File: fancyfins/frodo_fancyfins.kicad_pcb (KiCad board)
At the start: 2 copper layers, 140 x 115 mm, 102 parts, among them J3 TC2050, U1 AZ1117-5.0, U10 L78L05_SOT89, U11 W25Q128JVP, U12 L78L05_SOT89, U13 L78L05_SOT89, U14 L78L05_SOT89, U15 L78L05_SOT89, U16 L78L05_SOT89, U2 AZ1117-3.3, U3 STM32F103RCTx, U4 MCP2562-E-SN, U5 TPD4E1U06, U6 L78L05_SOT89, U7 L78L05_SOT89, U8 L78L05_SOT89, U9 L78L05_SOT89, Y1 8MHz 12pF

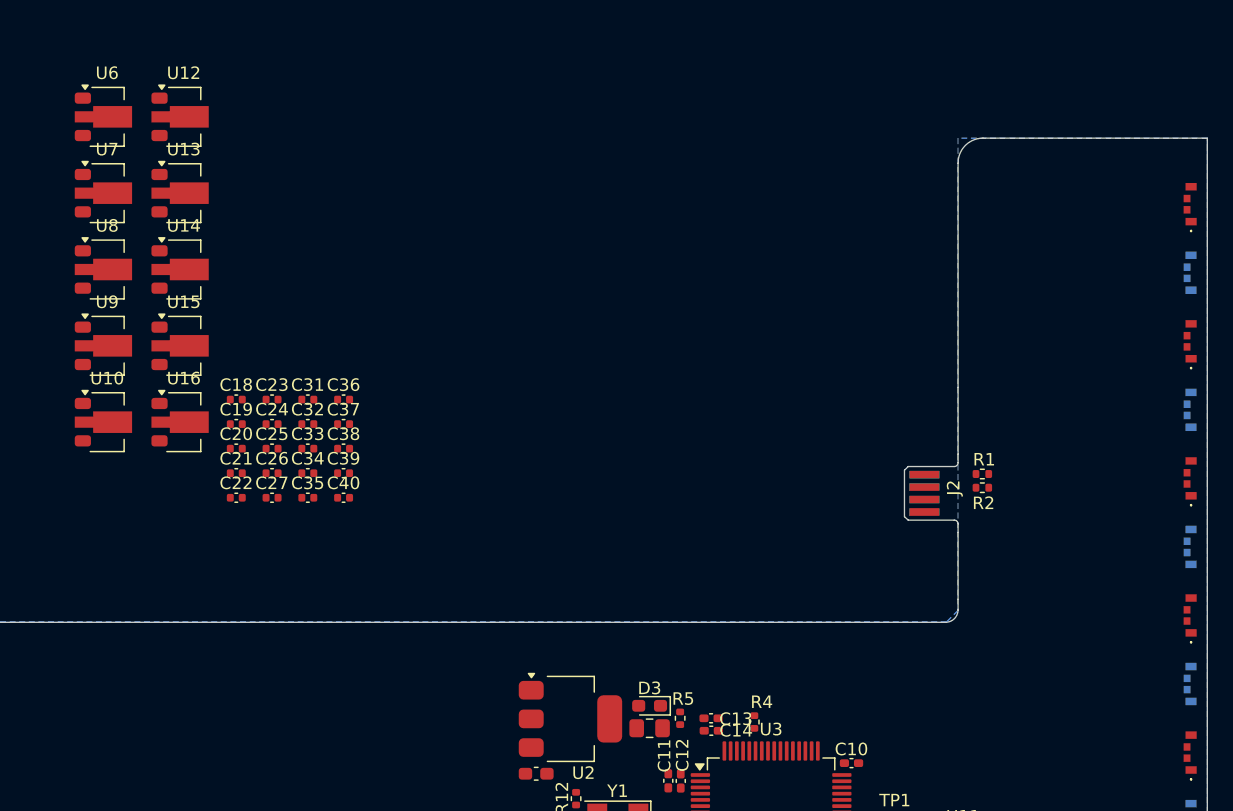
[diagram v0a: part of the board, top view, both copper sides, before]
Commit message: changed scematic + examplary layout
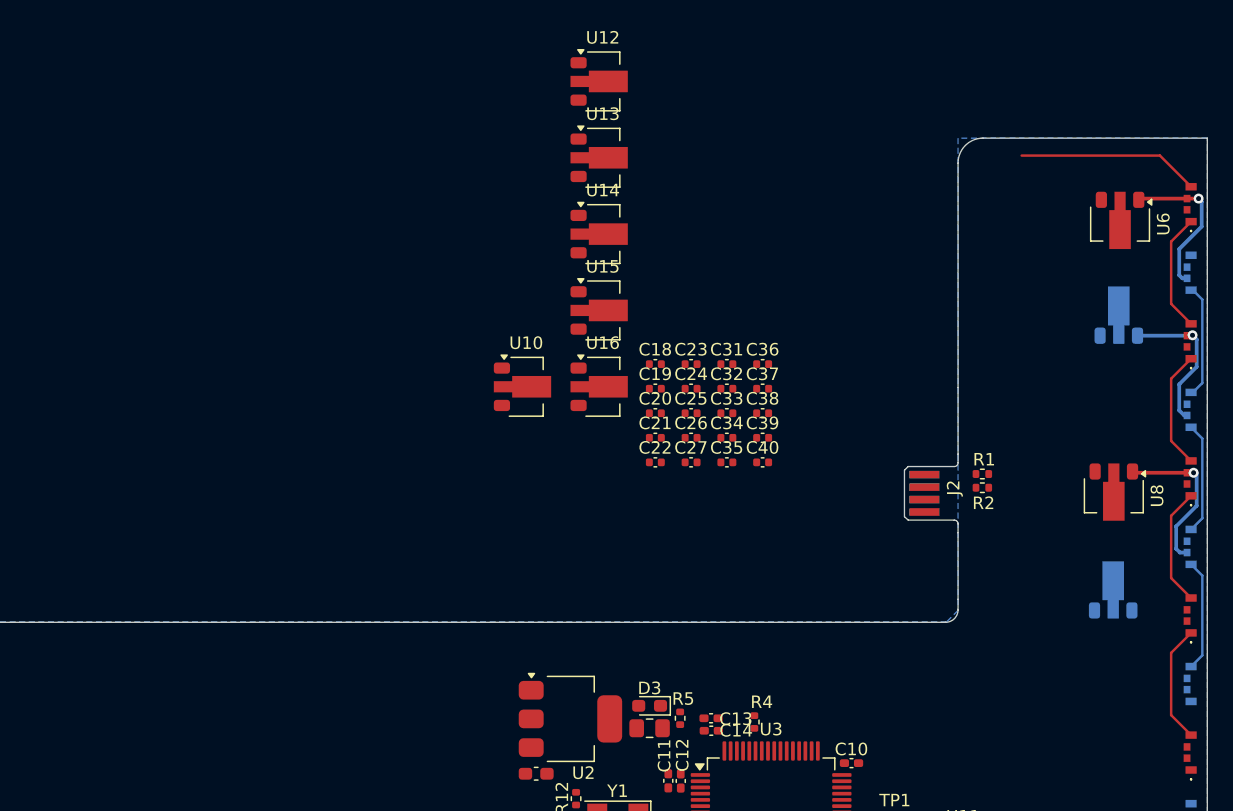
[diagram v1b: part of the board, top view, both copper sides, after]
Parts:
- U7, U9: moved to B.Cu
- moved U9 83.0 mm to (218.4, 71.0), turned to 90 degrees
- moved U8 82.8 mm to (218.5, 63.7), turned to -90 degrees
- moved U6 81.7 mm to (219.0, 41.9), turned to -90 degrees
- moved U7 81.7 mm to (218.9, 48.9), turned to 90 degrees
- moved C18 33.7 mm to (181.7, 53.1)
- moved C19 33.7 mm to (181.7, 55.1)
- moved C20 33.7 mm to (181.7, 57.1)
- moved C21 33.7 mm to (181.7, 59.0)
- moved C22 33.7 mm to (181.7, 61.0)
- moved C23 33.7 mm to (184.6, 53.1)
- moved C24 33.7 mm to (184.6, 55.1)
- moved C25 33.7 mm to (184.6, 57.1)
- moved C26 33.7 mm to (184.6, 59.0)
- moved C27 33.7 mm to (184.6, 61.0)
- moved C31 33.7 mm to (187.4, 53.1)
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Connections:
- D11 pad 4: Net-(D10-DO) -> Net-(D11-DIN)
- D12 pad 1: Net-(D12-DO) -> Net-(D10-DIN)
- D12 pad 4: Net-(D11-DO) -> Net-(D12-DIN)
- D13 pad 1: Net-(D13-DO) -> LED_Signal_cont
- D13 pad 4: Net-(D12-DO) -> Net-(D11-DO)
- D14 pad 1: LED_Signal_cont -> Net-(D12-DIN)
- D14 pad 4: Net-(D13-DO) -> LED_Signal_cont2
- D16 pad 1: Net-(D16-DO) -> LED_Signal_cont2
- D16 pad 4: Net-(D15-DO) -> Net-(D16-DIN)
- D17 pad 4: Net-(D16-DO) -> Net-(D15-DO)
- D18 pad 1: Net-(D18-DO) -> Net-(D16-DIN)
- D18 pad 4: Net-(D17-DO) -> Net-(D18-DIN)
- D19 pad 4: Net-(D18-DO) -> Net-(D17-DO)
- D20 pad 1: Net-(D20-DO) -> Net-(D18-DIN)
- D20 pad 4: Net-(D19-DO) -> Net-(D20-DIN)
- D21 pad 4: Net-(D20-DO) -> Net-(D19-DO)
- D22 pad 1: Net-(D22-DO) -> Net-(D20-DIN)
- D22 pad 4: Net-(D21-DO) -> Net-(D22-DIN)
- D23 pad 4: Net-(D22-DO) -> Net-(D21-DO)
- D24 pad 1: unconnected-(D24-DO-Pad1) -> Net-(D22-DIN)
- D6 pad 1: Net-(D6-DO) -> unconnected-(D6-DO-Pad1)
- D6 pad 4: Net-(D5-DO) -> Net-(D6-DIN)
- D7 pad 4: Net-(D6-DO) -> Net-(D5-DO)
- D8 pad 1: Net-(D8-DO) -> Net-(D6-DIN)
- D8 pad 4: Net-(D7-DO) -> Net-(D10-DO)
- D9 pad 1: Net-(D10-DIN) -> Net-(D11-DIN)
- D9 pad 4: Net-(D8-DO) -> Net-(D7-DO)
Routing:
- net LED_Signal: track 0.00 -> 14.6 mm
- net Net-(D10-VDD): track 0.00 -> 13.0 mm, vias 0 -> 1
- net Net-(D5-VDD): track 0.00 -> 12.6 mm, vias 0 -> 1
- net Net-(D7-VDD): track 0.00 -> 12.4 mm, vias 0 -> 1
- net Net-(D11-DO): track 0.00 -> 9.53 mm
- net Net-(D11-DIN): track 0.00 -> 9.53 mm
- net Net-(D7-DO): track 0.00 -> 9.53 mm
- net Net-(D5-DO): track 0.00 -> 9.53 mm
- net Net-(D6-DIN): track 0.00 -> 9.12 mm
- net Net-(D10-DIN): track 0.00 -> 8.95 mm
- net Net-(D10-DO): track 0.00 -> 8.95 mm

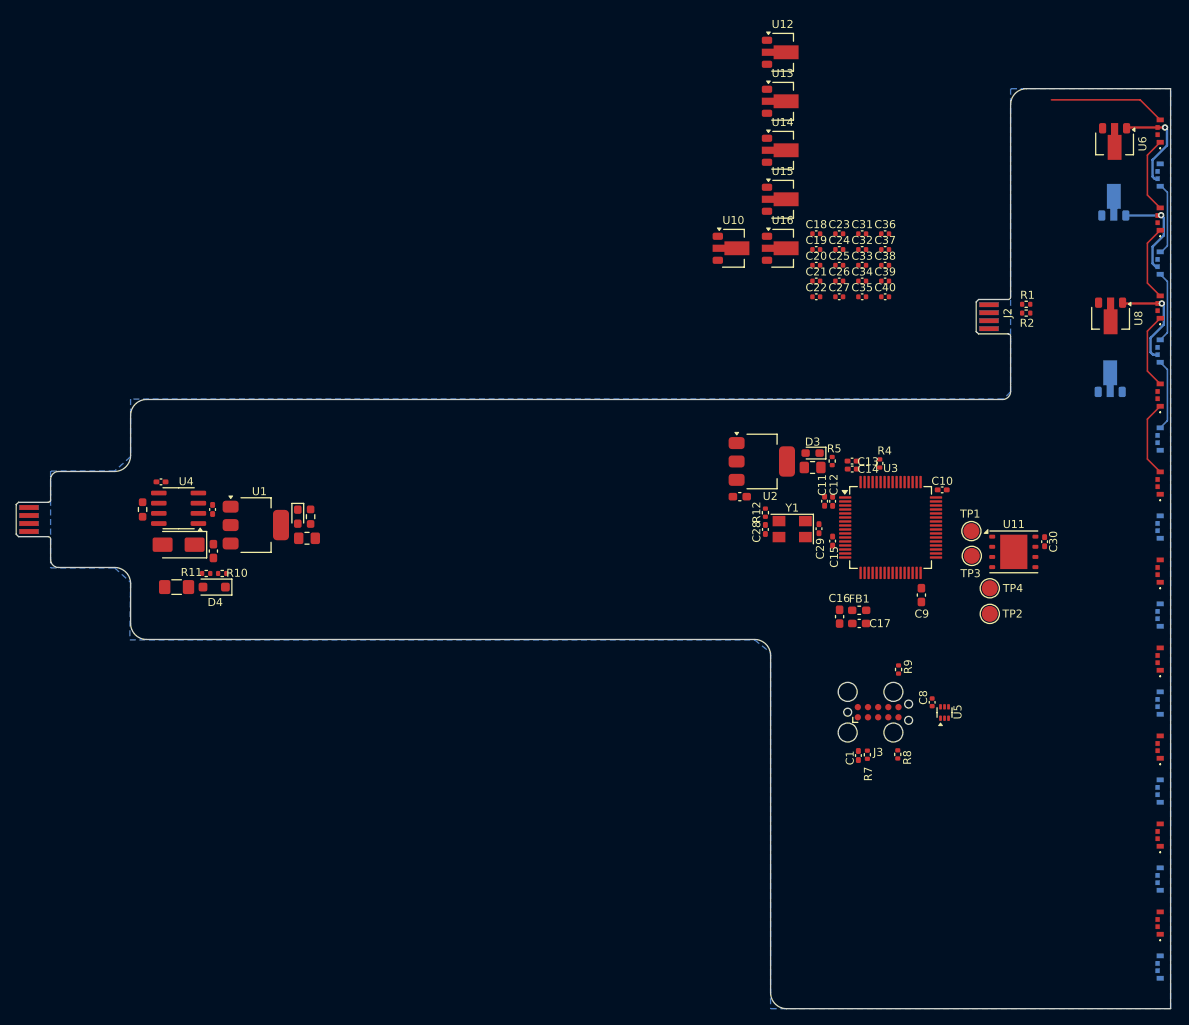
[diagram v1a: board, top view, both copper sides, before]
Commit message: began fancyfin routing
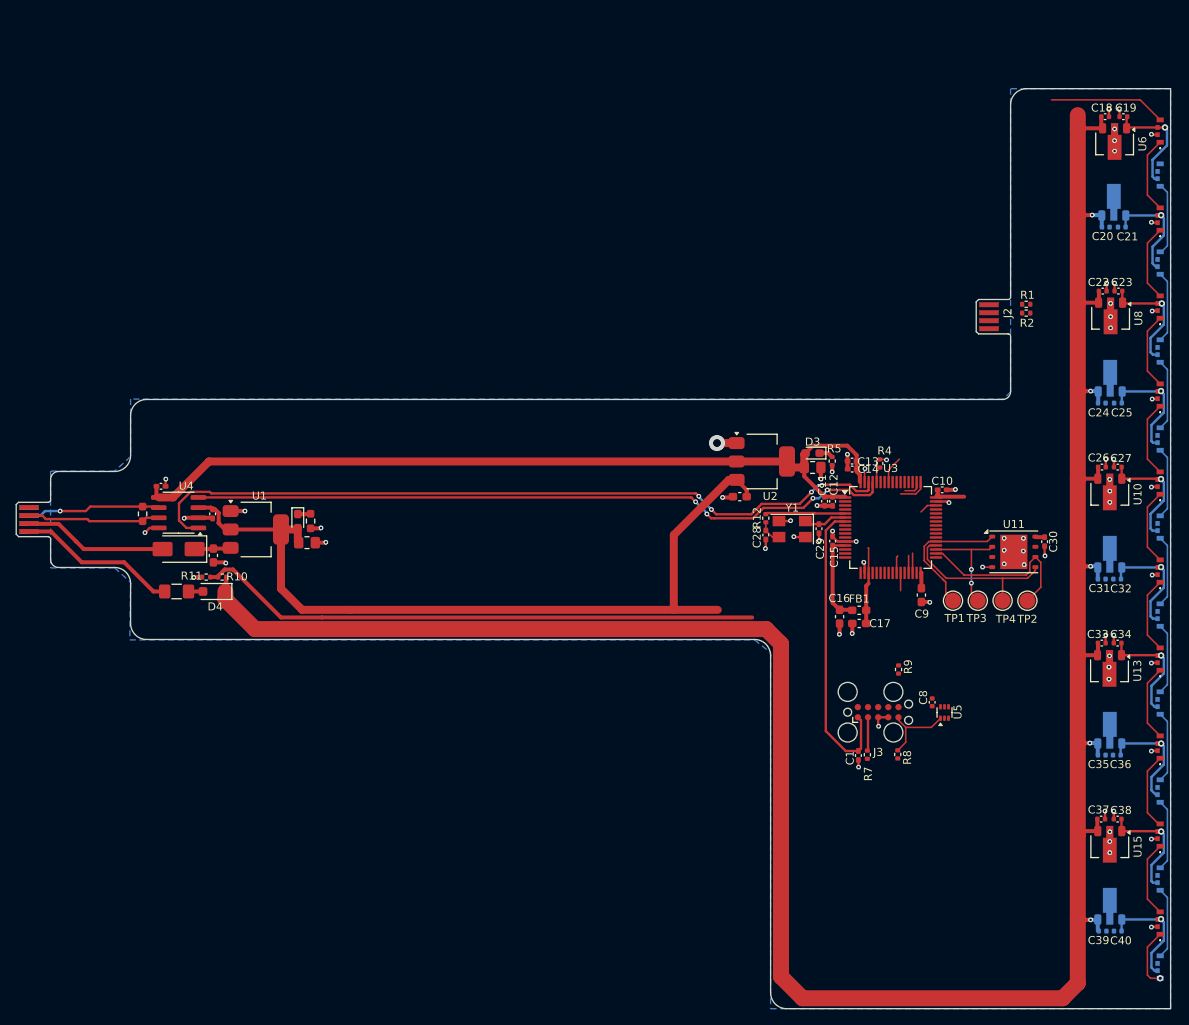
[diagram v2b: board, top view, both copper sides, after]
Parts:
- C20, C21, C24, C25, C31, C32, C35, C36, C39, C40, U12, U14, U16: moved to B.Cu
- moved U16 91.6 mm to (218.4, 136.9), turned to 90 degrees
- moved U15 90.7 mm to (218.4, 129.8), turned to -90 degrees
- moved C39 85.7 mm to (217.5, 140.3)
- moved C40 84.4 mm to (219.4, 140.3), turned to 180 degrees
- moved U14 83.0 mm to (218.4, 114.9), turned to 90 degrees
- moved U13 82.1 mm to (218.4, 107.8), turned to -90 degrees
- moved C37 76.1 mm to (217.3, 126.3)
- moved C38 75.1 mm to (219.4, 126.3), turned to 180 degrees
- moved U12 74.7 mm to (218.4, 92.9), turned to 90 degrees
- moved C36 71.3 mm to (219.3, 118.3), turned to 180 degrees
- moved C35 64.6 mm to (217.4, 118.3)
- moved U10 56.2 mm to (218.4, 85.7), turned to -90 degrees
- moved C33 55.9 mm to (217.4, 104.3)
- moved C34 55.4 mm to (219.4, 104.3), turned to 180 degrees
- moved C31 52.5 mm to (217.4, 96.3)
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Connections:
- J2 pad 4: unconnected-(J2-Pin_4-Pad4) -> P_A_Out
- U3 pad 26: unconnected-(U3-PB0-Pad26) -> P_A_Out
- U3 pad 50: unconnected-(U3-PA15-Pad50) -> SWO
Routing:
- net VD: track 0.00 -> 305.1 mm, vias 0 -> 5
- net +3.3V: track 0.00 -> 121.4 mm
- net +5V: track 0.00 -> 102.0 mm
- net CAN_TX: track 0.00 -> 95.8 mm, vias 0 -> 4
- net CAN_RX: track 0.00 -> 88.6 mm, vias 0 -> 4
- net VDsense: track 0.00 -> 72.9 mm
- net GND: track 0.00 -> 66.4 mm, vias 0 -> 73
- net NRST: track 0.00 -> 37.6 mm
- net SPI2_SCK: track 0.00 -> 21.6 mm
- net SPI2_MOSI: track 0.00 -> 20.8 mm
- net charging_voltage: track 0.00 -> 20.1 mm
- net Net-(D1-A): track 0.00 -> 18.1 mm
- net SPI_CS_FLASH: track 0.00 -> 17.6 mm
- net CAN_L_IN: track 0.00 -> 16.7 mm, vias 0 -> 1
- net CAN_H_IN: track 0.00 -> 16.7 mm
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
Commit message: continued working on fancyfins routing
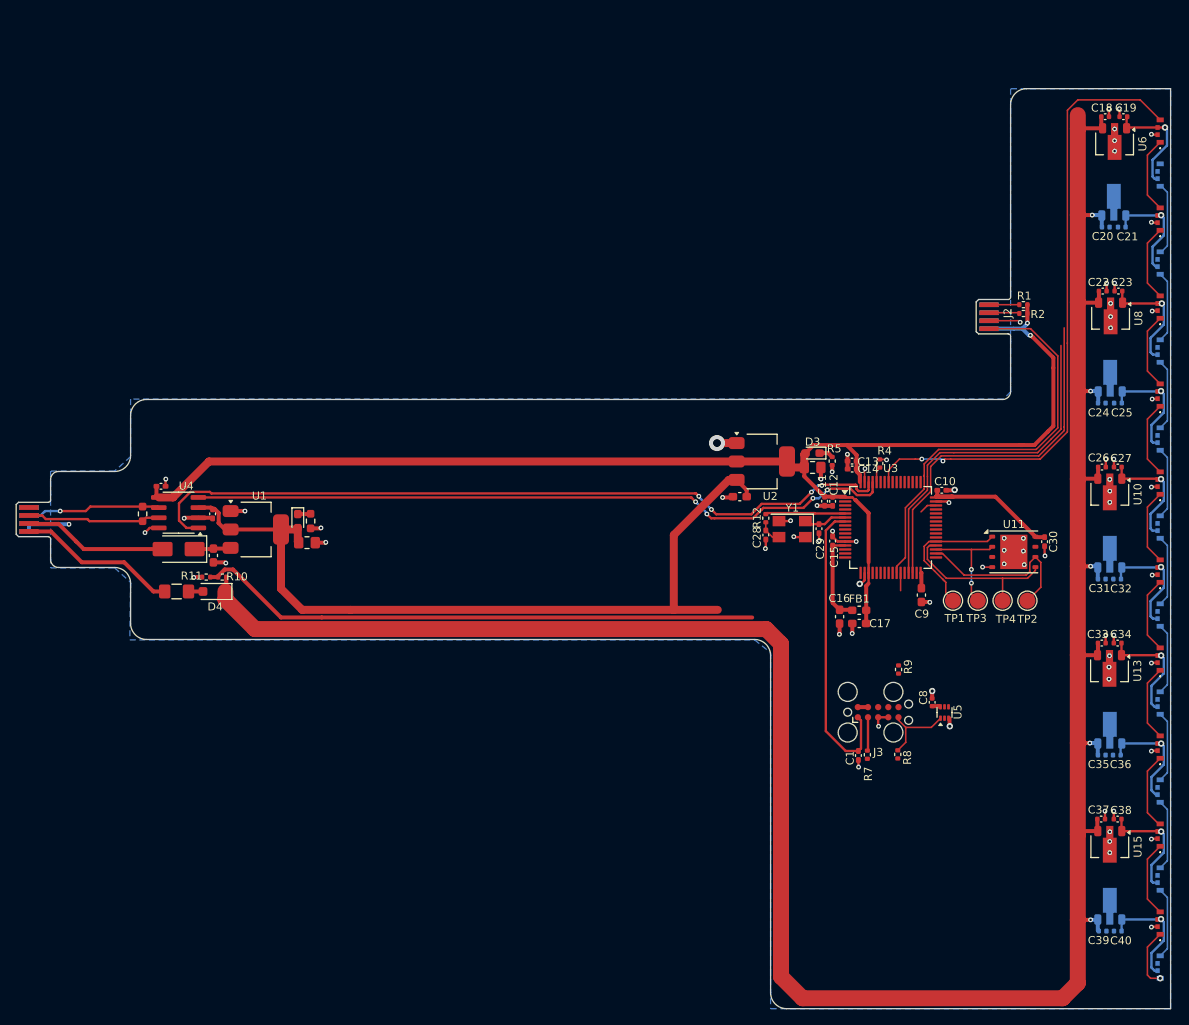
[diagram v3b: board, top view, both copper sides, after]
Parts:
- moved R2 0.35 mm to (207.6, 63.1)
- moved R1 0.35 mm to (207.6, 62.0)
- moved C10 0.07 mm to (197.4, 85.2)
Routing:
- net +3.3V: track 121.4 -> 190.5 mm, vias 0 -> 2
- net LED_Signal: track 18.1 -> 79.4 mm, vias 0 -> 2
- net P_A_Out: track 2.19 -> 52.7 mm
- net P_SDA: track 2.48 -> 49.5 mm
- net P_SCL: track 2.18 -> 47.4 mm
- net GND: track 66.4 -> 78.7 mm, vias 73 -> 77
- net SWCLK: track 3.62 -> 0.00 mm
- net SWO: track 2.37 -> 0.00 mm
- net +5V: track 102.0 -> 104.3 mm
